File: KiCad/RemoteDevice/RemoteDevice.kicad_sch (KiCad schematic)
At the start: 43 parts, among them J1 CN1, J2 Antenne, J3 Alim, Q1 Si4435, SW1 BP, SW2 BP, U1 STM32L041F6Px, U2 XC9140, U3 MCP6281, U4 ADT7410TRZ, U5 MCP6281, U6 RT606, U7 Microphone

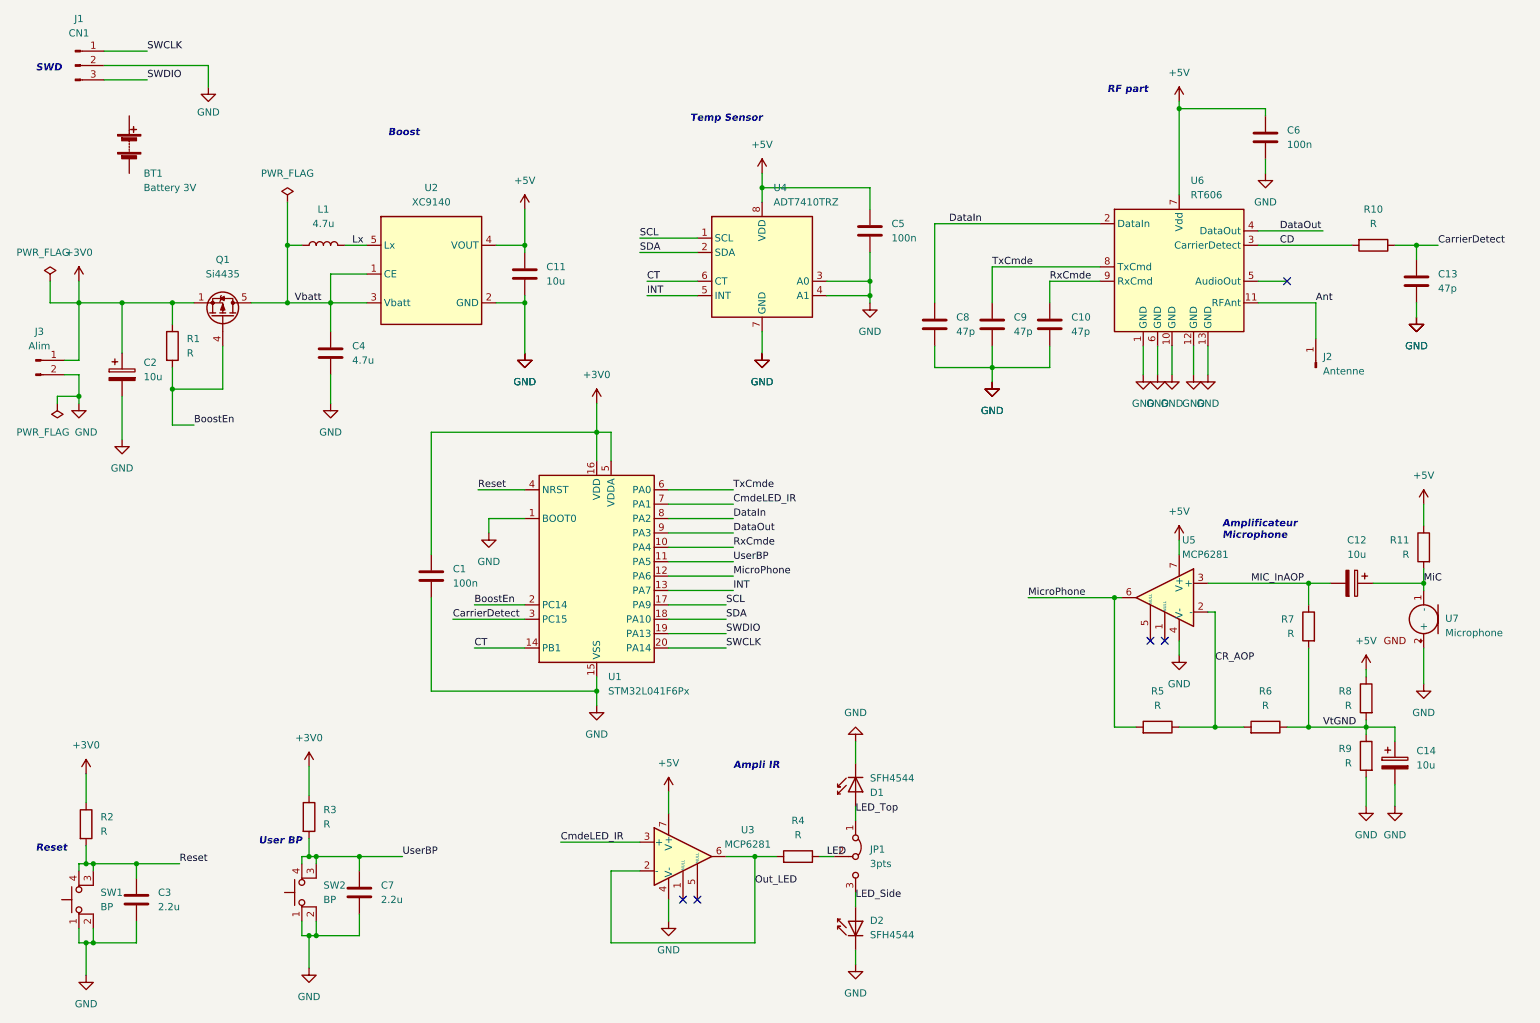
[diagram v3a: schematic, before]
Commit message: suppression des warning et erreurs, il en reste mais pas grave. Vérifier remap
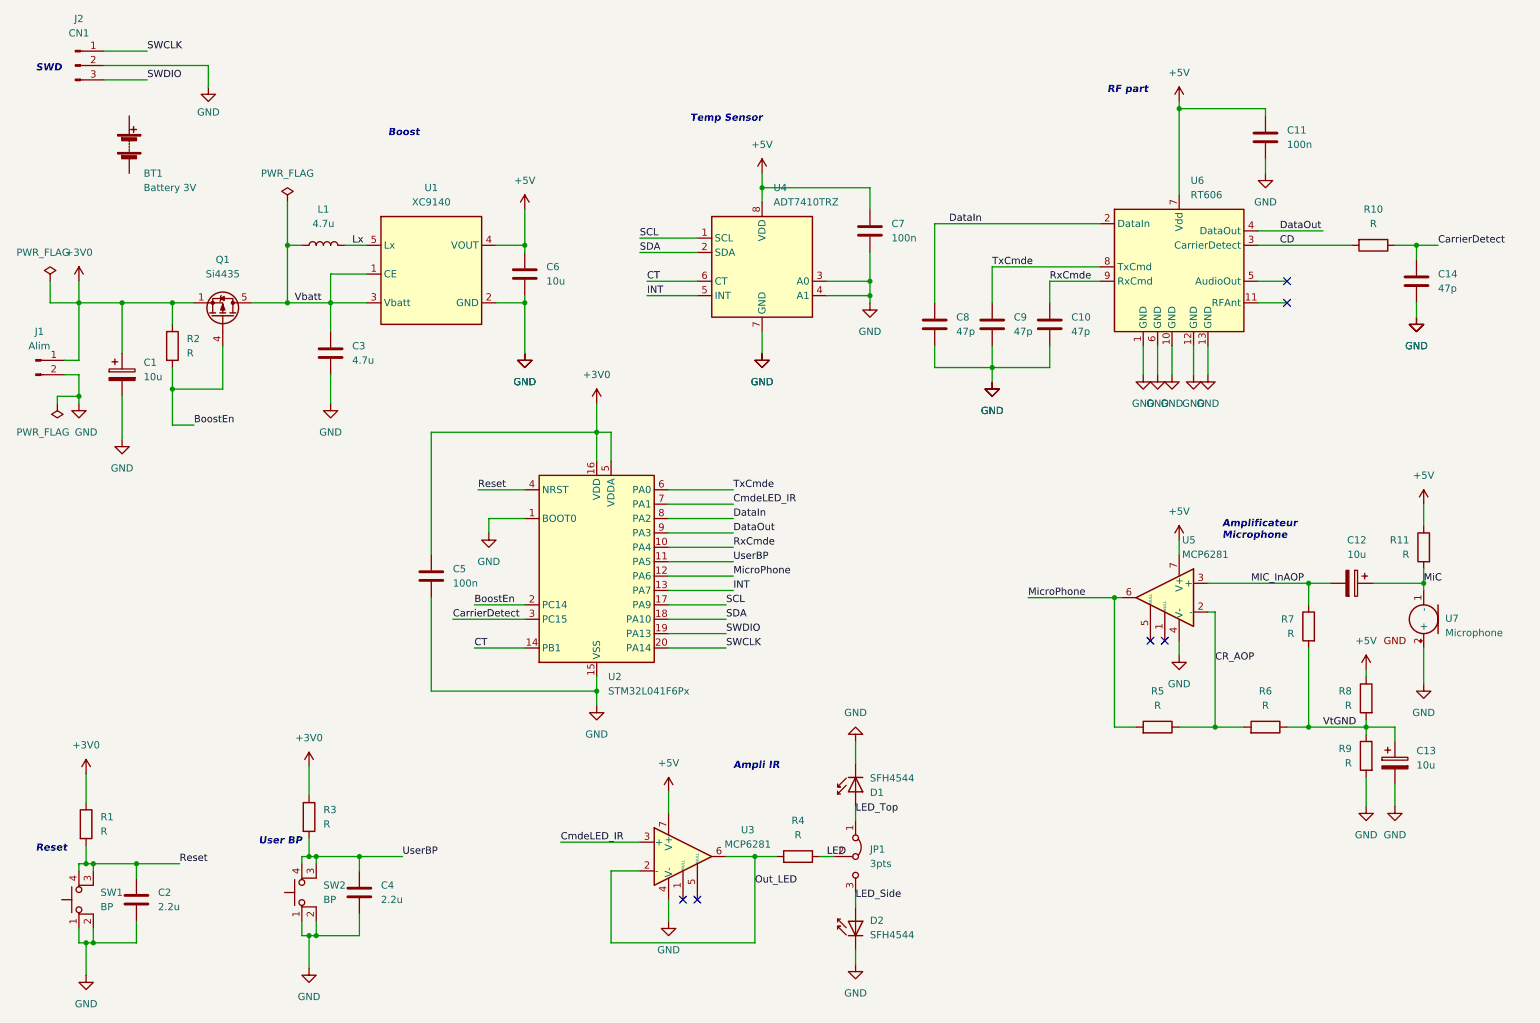
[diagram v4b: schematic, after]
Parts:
- removed J2: Antenne, Connector_PinHeader_1.00mm:PinHeader_1x01_P1.00mm_Vertical, symbol Connector:Conn_01x01_Male
- renumbered C2 to C1, C6 to C11, C14 to C13, C13 to C14, C3 to C2, C4 to C3, C7 to C4, C1 to C5, C11 to C6, C5 to C7, J3 to J1, J1 to J2, R2 to R1, R1 to R2, U2 to U1, U1 to U2
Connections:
- net Ant: no longer names the net of U6.11 (RFAnt)
- no-connect marks 5 -> 6
